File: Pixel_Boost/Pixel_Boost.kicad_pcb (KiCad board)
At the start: 2 copper layers, 28.8 x 14 mm, 9 parts, among them J1 In, J2 Out, U1 MCP1703A, U2 74LVC1G17

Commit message: added logo
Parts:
- added G***: LOGO, Scotts:chewi_15, B.Cu at (150.0, 113.1)
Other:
- board size 28.8 x 14 mm -> 28.5 x 14 mm
- board text added: "${TITLE} ${REVISION}"

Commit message: update
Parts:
- moved J2 1.14 mm to (160.0, 109.3)
- moved R2 1.13 mm to (155.7, 115.5)
- moved C3 0.95 mm to (153.3, 115.3)
- moved U2 0.93 mm to (149.7, 116.2)
- moved C1 0.80 mm to (146.9, 111.0)
- moved G*** 0.76 mm to (149.3, 113.1)
- moved C2 0.63 mm to (154.0, 108.7)
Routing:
- net +5V: track 14.6 -> 12.4 mm
- net Net-(R1-Pad2): track 2.72 -> 1.79 mm
- net GND: track 13.5 -> 12.8 mm
- net Net-(J2-Pad2): track 5.52 -> 5.00 mm
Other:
- board size 28.5 x 14 mm -> 27.2 x 14 mm

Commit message: change footprint
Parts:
- J1, J2: footprint Connector_Phoenix_MC:PhoenixContact_MCV_1,5_3-G-3.81_1x03_P3.81mm_Vertical -> Scotts:PhoenixContact_MCV_1,5_3-G-3.81_1x03_P3.81mm_Vertical
- U1: value MCP1703A -> MCP1703A-SOT89
- moved C3 1.08 mm to (152.7, 114.5), turned to 90 degrees
- moved C2 0.64 mm to (154.0, 109.3)
- moved U1 0.64 mm to (150.4, 110.0)
- moved R2 0.11 mm to (155.6, 115.5)
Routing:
- net GND: track 12.8 -> 12.0 mm, vias 7 -> 8

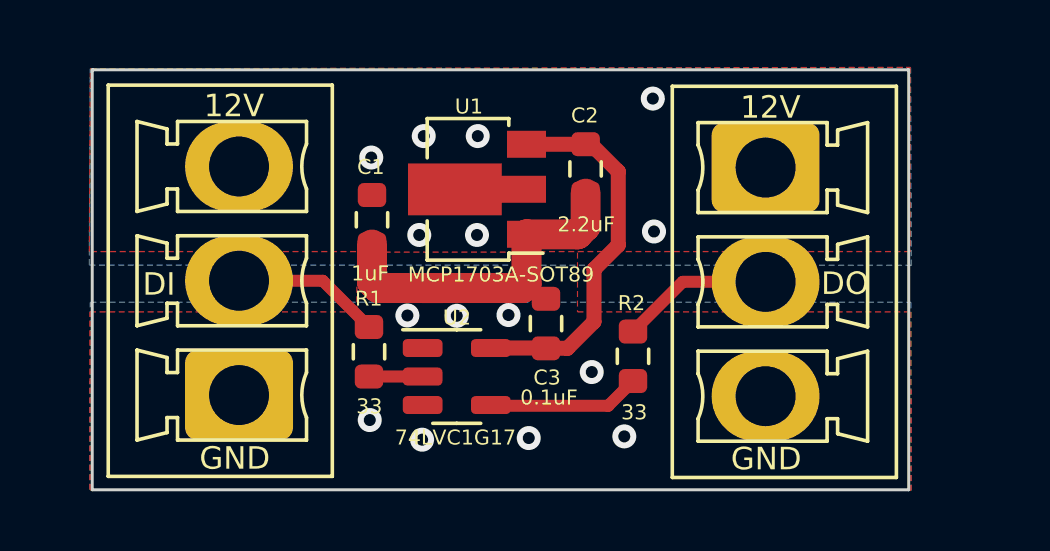
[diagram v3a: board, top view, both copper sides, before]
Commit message: add plug in 3 to 4 adapter
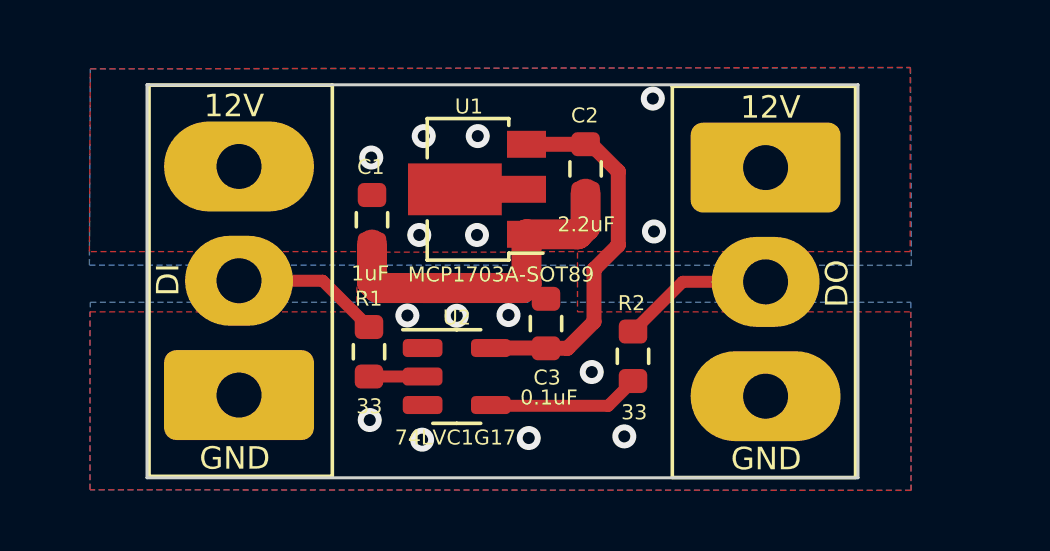
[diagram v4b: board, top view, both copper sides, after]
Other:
- board size 27.2 x 14 mm -> 23.7 x 13.1 mm
